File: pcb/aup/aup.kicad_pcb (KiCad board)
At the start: 6 copper layers, 100 x 80 mm, 95 parts, among them IC1 MT41K128M16JT-125_K, IC2 88E1512-A0-NNP2C000, J1 DF40C-100DS-0.4V_51, J2 DF40C-100DS-0.4V_51, J3 DF40C-100DS-0.4V_51, J4 DF40C-100DS-0.4V_51, Q1 AO3401A, Q2 AO3401A, U1 XC7A50T-FGG484, U11 FT2232HQ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

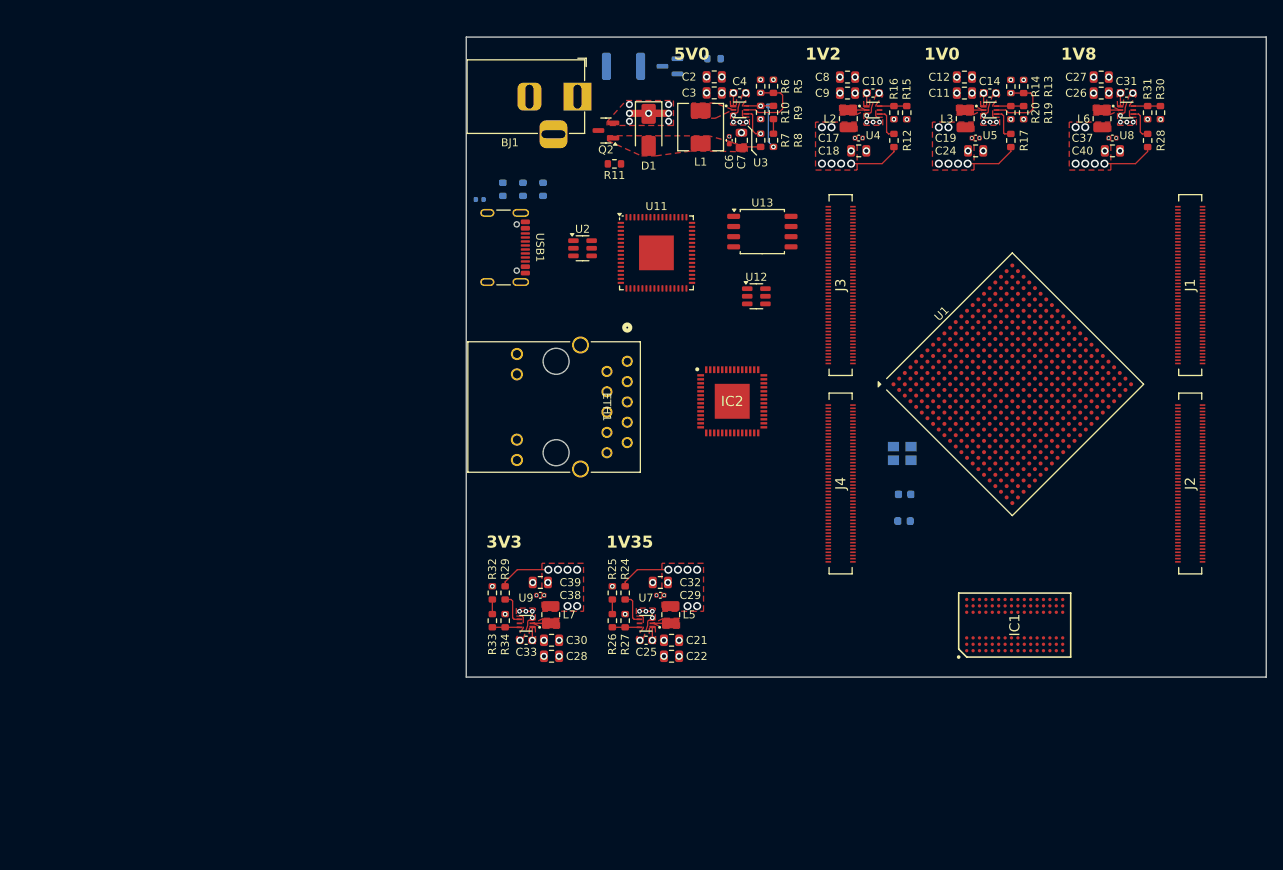
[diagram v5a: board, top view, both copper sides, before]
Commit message: Add some todo's on schematic. Add vias to fpga
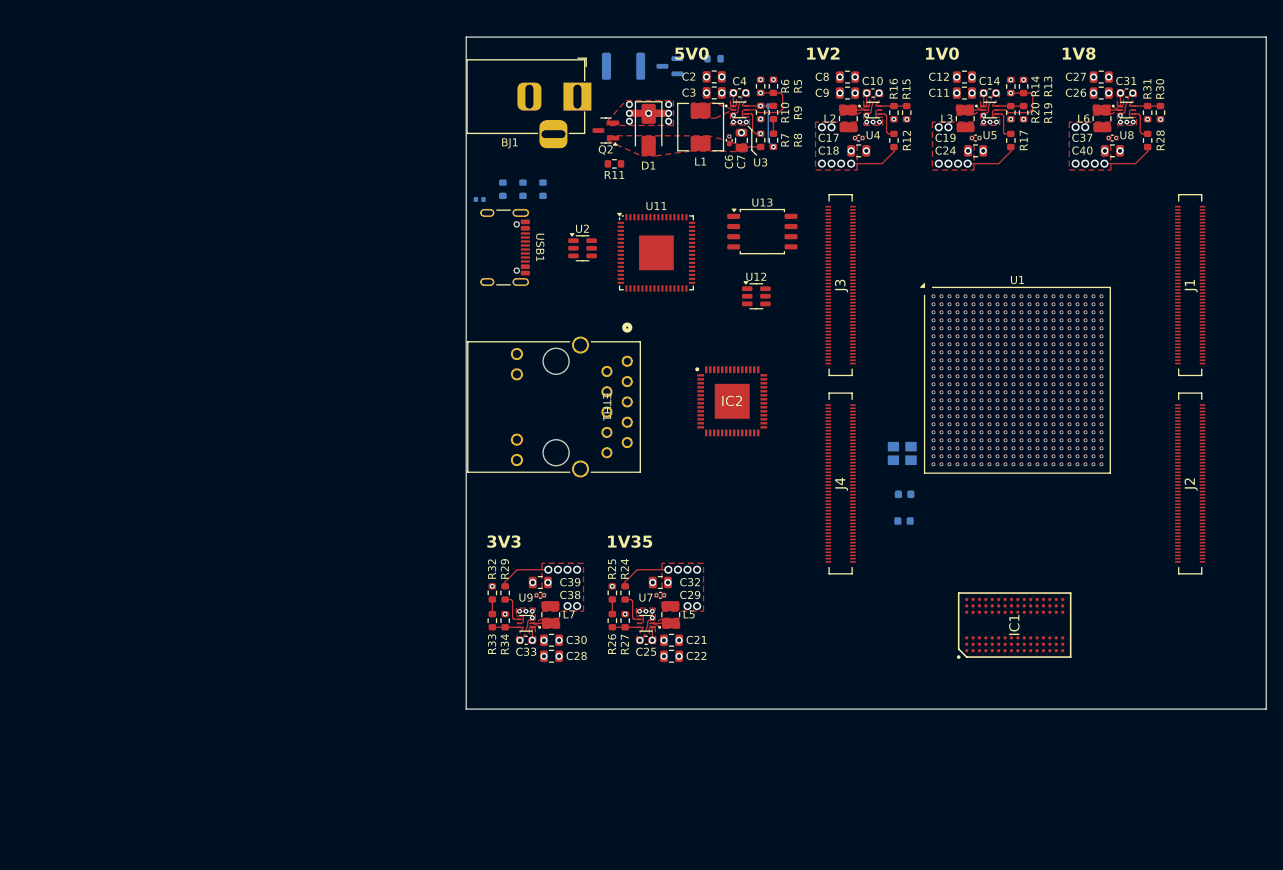
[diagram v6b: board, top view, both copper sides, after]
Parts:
- moved U1 0.81 mm to (168.9, 92.9), turned to 0 degrees
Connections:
- U1 pad H10: unconnected-(U1G-VCCINT-PadH10) -> +Vccint
- U1 pad H8: unconnected-(U1G-VCCINT-PadH8) -> +Vccint
- U1 pad J7: unconnected-(U1G-VCCINT-PadJ7) -> +Vccint
- U1 pad J9: unconnected-(U1G-VCCINT-PadJ9) -> +Vccint
- U1 pad K8: unconnected-(U1G-VCCINT-PadK8) -> +Vccint
- U1 pad L7: unconnected-(U1G-VCCINT-PadL7) -> +Vccint
- U1 pad M8: unconnected-(U1G-VCCINT-PadM8) -> +Vccint
- U1 pad N7: unconnected-(U1G-VCCINT-PadN7) -> +Vccint
- U1 pad P10: unconnected-(U1G-VCCINT-PadP10) -> +Vccint
- U1 pad P8: unconnected-(U1G-VCCINT-PadP8) -> +Vccint
- U1 pad R7: unconnected-(U1G-VCCINT-PadR7) -> +Vccint
- U1 pad R9: unconnected-(U1G-VCCINT-PadR9) -> +Vccint
- U1 pad T10: unconnected-(U1G-VCCINT-PadT10) -> +Vccint
- U1 pad T8: unconnected-(U1G-VCCINT-PadT8) -> +Vccint
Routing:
- net unconnected-(U1G-GND-PadA22): vias 0 -> 88
- net unconnected-(U1B-VCCO_16-PadF22): vias 0 -> 66
- net unconnected-(U1B-IO_L24N_T3_16-PadG22): vias 0 -> 44
- net unconnected-(U1B-IO_L22P_T3_16-PadE22): vias 0 -> 66
- net unconnected-(U1B-IO_L22N_T3_16-PadD22): vias 0 -> 66
- net unconnected-(U1B-IO_L20P_T3_16-PadC22): vias 0 -> 66
- net unconnected-(U1B-IO_L20N_T3_16-PadB22): vias 0 -> 88
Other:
- board size 100 x 80 mm -> 100 x 84 mm
- board text added: "do rough power route from the fpga to see if 5v0 should be where3v3 is. then put a power mux between 1v8 and 3v3 in the upper right. add resistor overrides for voltages on bottom"

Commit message: Redid bga vias
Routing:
- net +3V3: track 13.5 -> 6.58 mm
- net +1V35: track 13.5 -> 6.58 mm
- net /ext_power/REG_5V4: track 13.7 -> 7.67 mm
- net unconnected-(U1G-VCCBRAM-PadN11): vias 0 -> 1
- net unconnected-(U1G-VCCBRAM-PadL11): vias 0 -> 1
- net unconnected-(U1G-VCCBRAM-PadJ11): vias 0 -> 1
- net unconnected-(U1G-VCCBATT_0-PadE12): vias 0 -> 1
- net unconnected-(U1G-VCCAUX-PadR11): vias 0 -> 1
- net unconnected-(U1G-VCCAUX-PadP12): vias 0 -> 1
- net unconnected-(U1G-VCCAUX-PadM12): vias 0 -> 1
- net unconnected-(U1G-VCCAUX-PadK12): vias 0 -> 1
- net unconnected-(U1G-VCCAUX-PadH12): vias 0 -> 1
- net unconnected-(U1G-VCCADC_0-PadK10): vias 0 -> 1
- net unconnected-(U1G-GNDADC_0-PadK9): vias 0 -> 1
- net unconnected-(U1G-GND-PadY5): vias 0 -> 1
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
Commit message: Start to add net class color
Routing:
- net +Vccint: track 14.5 -> 58.4 mm
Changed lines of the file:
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@@
+	)
+	(segment
+		(start 165.4 95.4)
+		(end 164.4 96.4)
+		(width 0.156464)
+		(layer "In2.Cu")
+		(net 754)
+	)
+	(segment
+		(start 165.4 91.4)
+		(end 164.4 90.400001)
+		(width 0.156464)
+		(layer "In2.Cu")
+		(net 754)
+	)
+	(segment
+		(start 164.4 94.4)
+		(end 165.4 93.4)
+		(width 0.156464)
+		(layer "In2.Cu")
+		(net 754)
+	)
+	(segment
+		(start 164.4 92.4)
+		(end 165.4 91.4)
+		(width 0.156464)
+		(layer "In2.Cu")
+		(net 754)
+	)
+	(segment
+		(start 167.4 97.4)
+		(end 166.4 96.4)
+		(width 0.156464)
+		(layer "In2.Cu")
+		(net 754)
+	)
+	(segment
+		(start 166.9 88.9)
+		(end 166.9 70.048348)
+		(width 0.156464)
+		(layer "In2.Cu")
+		(net 754)
+	)
+	(segment
+		(start 167.4 95.4)
+		(end 166.4 96.4)
+		(width 0.156464)
+		(layer "In2.Cu")
+		(net 754)
+	)
+	(segment
+		(start 166.4 96.4)
+		(end 165.4 95.4)
+		(width 0.156464)
+		(layer "In2.Cu")
+		(net 754)
+	)
+	(segment
+		(start 167.4 89.4)
+		(end 166.9 88.9)
+		(width 0.156464)
+		(layer "In2.Cu")
+		(net 754)
+	)
+	(segment
+		(start 164.4 90.400001)
+		(end 165.4 89.4)
+		(width 0.156464)
+		(layer "In2.Cu")
+		(net 754)
+	)
+	(segment
+		(start 165.4 93.4)
+		(end 164.4 92.4)
+		(width 0.156464)
+		(layer "In2.Cu")
+		(net 754)
+	)
+	(segment
+		(start 165.4 95.4)
+		(end 164.4 94.4)
+		(width 0.156464)
+		(layer "In2.Cu")
+		(net 754)
+	)
+	(segment
+		(start 166.4 90.4)
+		(end 167.4 89.4)
+		(width 0.156464)
+		(layer "In2.Cu")
+		(net 754)
+	)
+	(segment
+		(start 166.9 70.048348)
+		(end 162.675 65.823348)
+		(width 0.156464)
+		(layer "In2.Cu")
+		(net 754)
+	)
+	(segment
+		(start 165.4 91.4)
+		(end 166.4 90.4)
+		(width 0.156464)
+		(layer "In2.Cu")
+		(net 754)
+	)
+	(segment
+		(start 166.4 96.4)
+		(end 165.4 97.4)
+		(width 0.156464)
+		(layer "In2.Cu")
+		(net 754)
 	)
 	(segment
